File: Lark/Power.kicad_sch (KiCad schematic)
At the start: 48 parts, among them J1 54-00128, Q1 MMBT2222A-7-F, Q2 MMBT2222A-7-F, U5 SQM120P06-07L_GE3, U6 BD9E302EFJ-E2, U7 SI3474DV-T1-BE3, U8 BD9G102G-LBTR, U9 LD39200PU33R

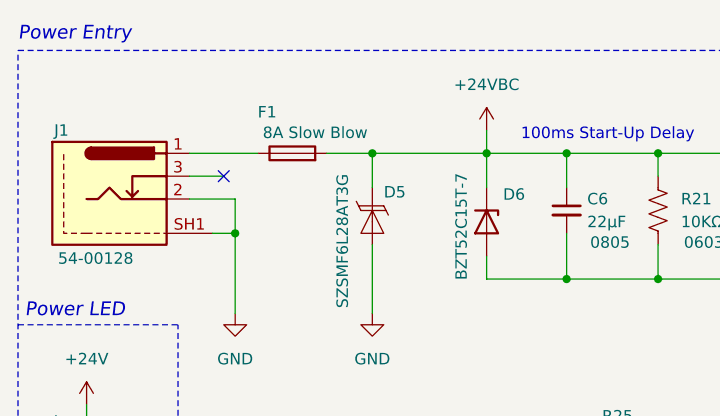
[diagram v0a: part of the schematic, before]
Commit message: Finishing up the layout, WIP
- Changed USBC footprint silkscreen.
- Routed Power Section.
- Switched from 7A to 10A Fuse.
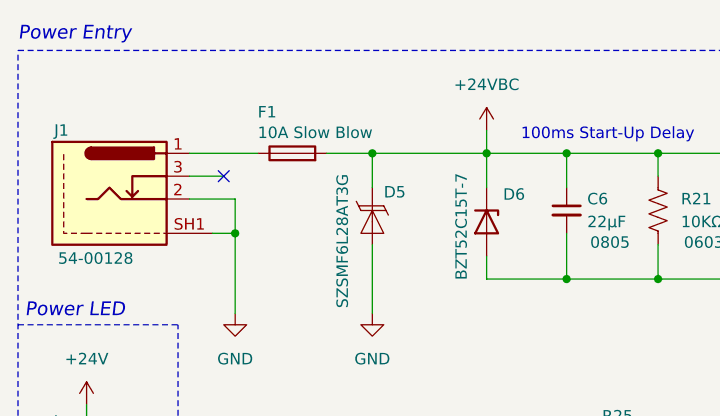
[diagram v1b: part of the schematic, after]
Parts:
- F1: value 8A Slow Blow -> 10A Slow Blow; MPN 3413.0326.22 -> 3413.0328.22
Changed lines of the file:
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@@
 			)
 		)
-		(property "Value" "8A Slow Blow"
+		(property "Value" "10A Slow Blow"
 			(at 48.26 33.274 90)
 			(effects
@@
 			)
 		)
-		(property "MPN" "3413.0326.22"
+		(property "MPN" "3413.0328.22"
 			(at 60.96 35.56 0)
 			(effects

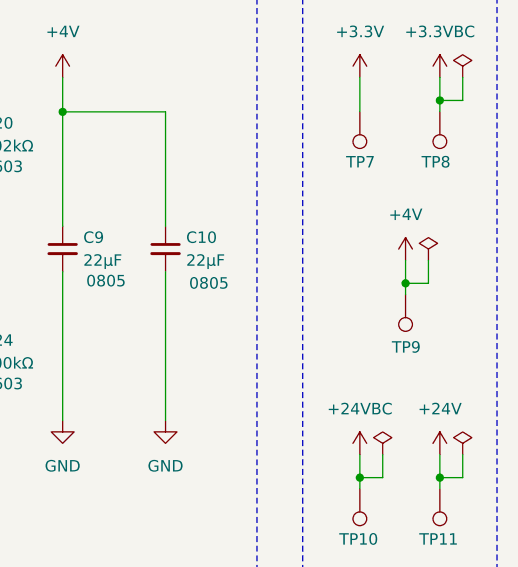
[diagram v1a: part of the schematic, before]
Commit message: minor updates
- changed npn pins to passive.
- changed rev to match working revision.
- minor PCB changes.
- moved TVS diode next to connector.
- changed barrel jack silkscreen.
- changed usbc silkscreen.
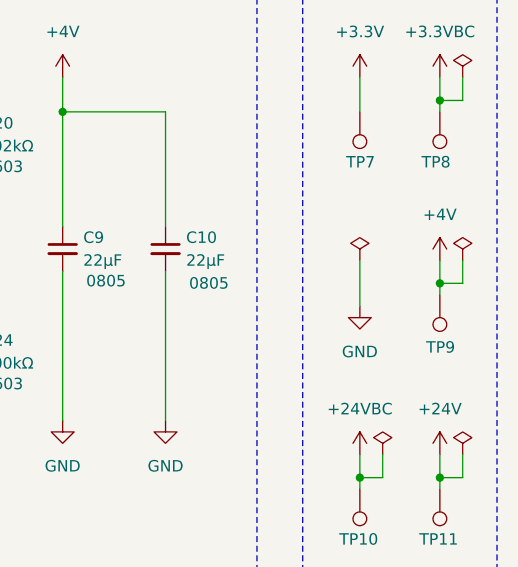
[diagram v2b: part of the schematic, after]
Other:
- moved on the sheet: TP9
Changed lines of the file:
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@@
 		(title "Lark Print Engine")
 		(date "2025-10-08")
-		(rev "01.00.01")
+		(rev "01.00.00")
 		(comment 1 "Thermal Print Engine")
 		(comment 2 "Designer: HamSlices")
@@
 	)
 	(junction
-		(at 270.51 55.88)
+		(at 274.32 55.88)
 		(diameter 0)
 		(color 0 0 0 0)
@@
 	(wire
 		(pts
-			(xy 273.05 53.34) (xy 273.05 55.88)
+			(xy 276.86 53.34) (xy 276.86 55.88)
 		)
 		(stroke
@@
 	(wire
 		(pts
-			(xy 273.05 55.88) (xy 270.51 55.88)
+			(xy 276.86 55.88) (xy 274.32 55.88)
 		)
 		(stroke
@@
 	(wire
 		(pts
-			(xy 270.51 53.34) (xy 270.51 55.88)
+			(xy 274.32 53.34) (xy 274.32 55.88)
 		)
 		(stroke
@@
 	(wire
 		(pts
-			(xy 270.51 55.88) (xy 270.51 57.15)
+			(xy 274.32 55.88) (xy 274.32 57.15)
 		)
 		(stroke
@@
 	(wire
 		(pts
+			(xy 265.43 53.34) (xy 265.43 58.42)
+		)
+		(stroke
+			(width 0)
+			(type default)
+		)
+	)
+	(wire
+		(pts
 			(xy 100.33 148.59) (xy 100.33 152.4)
 		)
@@
 	)
 	(symbol
+		(lib_id "power:PWR_FLAG")
+		(at 265.43 53.34 0)
+		(unit 1)
+		(exclude_from_sim no)
+		(in_bom yes)
+		(on_board yes)
+		(dnp no)
+		(fields_autoplaced yes)
+		(property "Reference" "#FLG07"
+			(at 265.43 51.435 0)
+			(effects
+				(font
+					(size 1.27 1.27)
+				)
+				(hide yes)
+			)
+		)
+		(property "Value" "PWR_FLAG"
+			(at 265.43 48.26 0)
+			(effects
+				(font
+					(size 1.27 1.27)
+				)
+				(hide yes)
+			)
+		)
+		(property "Footprint" ""
+			(at 265.43 53.34 0)
+			(effects
+				(font
+					(size 1.27 1.27)
+				)
+				(hide yes)
+			)
+		)
+		(property "Datasheet" "~"
+			(at 265.43 53.34 0)
+			(effects
+				(font
+					(size 1.27 1.27)
+				)
+				(hide yes)
+			)
+		)
+		(property "Description" "Special symbol for telling ERC where power comes from"
+			(at 265.43 53.34 0)
+			(effects
+				(font
+					(size 1.27 1.27)
+				)
+				(hide yes)
+			)
+		)
+		(pin "1"
+		)
+		(instances
+			(project "Lark"
+				(path "/a351af57-4353-47da-9f45-7393de572768/e2a48b8e-2a6a-42c1-ac2d-aa8bef5f3773"
+					(reference "#FLG07")
+					(unit 1)
+				)
+			)
+		)
+	)
+	(symbol
 		(lib_id "power:GND")
 		(at 218.44 152.4 0)
@@
 	)
 	(symbol
+		(lib_name "MMBT2222A-7-F_1")
 		(lib_id "Diodes Incorporated:MMBT2222A-7-F")
 		(at 215.9 144.78 0)
@@
 	(symbol
 		(lib_id "power:+3.3V")
-		(at 270.51 53.34 0)
+		(at 274.32 53.34 0)
 		(unit 1)
 		(exclude_from_sim no)
@@
 		(fields_autoplaced yes)
 		(property "Reference" "#PWR047"
-			(at 270.51 57.15 0)
+			(at 274.32 57.15 0)
 			(effects
 				(font
@@
 		)
 		(property "Value" "+4V"
-			(at 270.51 48.26 0)
+			(at 274.32 48.26 0)
 			(effects
 				(font
@@
 		)
 		(property "Footprint" ""
-			(at 270.51 53.34 0)
+			(at 274.32 53.34 0)
 			(effects
 				(font
@@
 		)
 		(property "Datasheet" ""
-			(at 270.51 53.34 0)
+			(at 274.32 53.34 0)
 			(effects
 				(font
@@
 		)
 		(property "Description" "Power symbol creates a global label with name \"+3.3V\""
-			(at 270.51 53.34 0)
+			(at 274.32 53.34 0)
 			(effects
 				(font
@@
 	)
 	(symbol
+		(lib_id "power:GND")
+		(at 265.43 58.42 0)
+		(unit 1)
+		(exclude_from_sim no)
+		(in_bom yes)
+		(on_board yes)
+		(dnp no)
+		(fields_autoplaced yes)
+		(property "Reference" "#PWR0186"
+			(at 265.43 64.77 0)
+			(effects
+				(font
+					(size 1.27 1.27)
+				)
+				(hide yes)
+			)
+		)
+		(property "Value" "GND"
+			(at 265.43 63.5 0)
+			(effects
+				(font
+					(size 1.27 1.27)
+				)
+			)
+		)
+		(property "Footprint" ""
+			(at 265.43 58.42 0)
+			(effects
+				(font
+					(size 1.27 1.27)
+				)
+				(hide yes)
+			)
+		)
+		(property "Datasheet" ""
+			(at 265.43 58.42 0)
+			(effects
+				(font
+					(size 1.27 1.27)
+				)
+				(hide yes)
+			)
+		)
+		(property "Description" "Power symbol creates a global label with name \"GND\" , ground"
+			(at 265.43 58.42 0)
+			(effects
+				(font
+					(size 1.27 1.27)
+				)
+				(hide yes)
+			)
+		)
+		(pin "1"
+		)
+		(instances
+			(project "Lark"
+				(path "/a351af57-4353-47da-9f45-7393de572768/e2a48b8e-2a6a-42c1-ac2d-aa8bef5f3773"
+					(reference "#PWR0186")
+					(unit 1)
+				)
+			)
+		)
+	)
+	(symbol
 		(lib_id "Stackpole:Resistor")
 		(at 100.33 156.21 0)
@@
 	(symbol
 		(lib_id "power:PWR_FLAG")
-		(at 273.05 53.34 0)
+		(at 276.86 53.34 0)
 		(unit 1)
 		(exclude_from_sim no)
@@
 		(fields_autoplaced yes)
 		(property "Reference" "#FLG02"
-			(at 273.05 51.435 0)
+			(at 276.86 51.435 0)
 			(effects
 				(font
@@
 		)
 		(property "Value" "PWR_FLAG"
-			(at 273.05 48.26 0)
+			(at 276.86 48.26 0)
 			(effects
 				(font
@@
 		)
 		(property "Footprint" ""
-			(at 273.05 53.34 0)
+			(at 276.86 53.34 0)
 			(effects
 				(font
@@
 		)
 		(property "Datasheet" "~"
-			(at 273.05 53.34 0)
+			(at 276.86 53.34 0)
 			(effects
 				(font
@@
 		)
 		(property "Description" "Special symbol for telling ERC where power comes from"
-			(at 273.05 53.34 0)
+			(at 276.86 53.34 0)
 			(effects
 				(font
@@
 	(symbol
 		(lib_id "Connector:TestPoint")
-		(at 270.51 57.15 180)
+		(at 274.32 57.15 180)
 		(unit 1)
 		(exclude_from_sim no)
@@
 		(dnp no)
 		(property "Reference" "TP9"
-			(at 268.986 62.992 0)
+			(at 272.796 62.992 0)
 			(effects
 				(font
@@
 		)
 		(property "Value" "TestPoint"
-			(at 268.986 65.532 0)
+			(at 272.796 65.532 0)
 			(effects
 				(font
@@
 		)
 		(property "Footprint" "TestPoint:TestPoint_Pad_D1.0mm"
-			(at 265.43 57.15 0)
+			(at 269.24 57.15 0)
 			(effects
 				(font
@@
 		)
 		(property "Datasheet" "~"
-			(at 265.43 57.15 0)
+			(at 269.24 57.15 0)
 			(effects
 				(font
@@
 		)
 		(property "Description" "test point"
-			(at 270.51 57.15 0)
+			(at 274.32 57.15 0)
 			(effects
 				(font

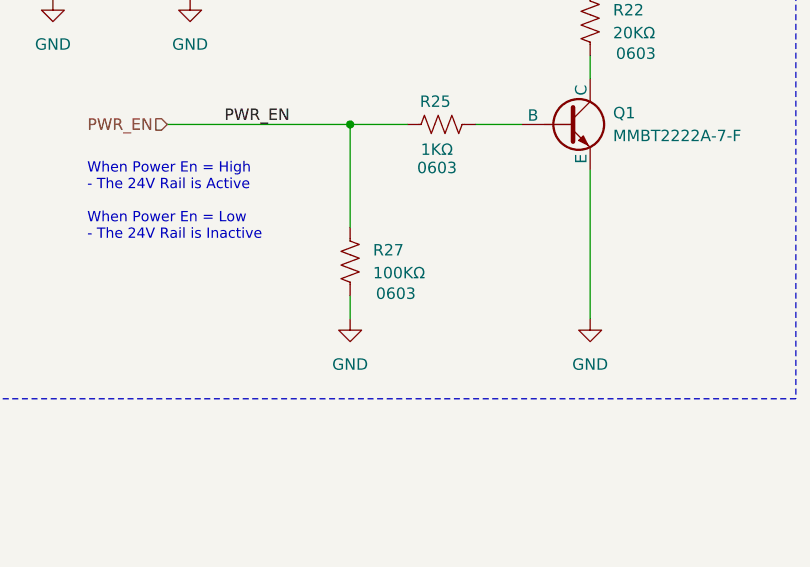
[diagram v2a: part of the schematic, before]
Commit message: Changed revision again...
- It dawned on me that this is rev 2, so the rev is now 01.00.1.
- Added thermal relief to the TH pads so I can actually solder the parts.
- Added more silkscreen to denote the rev, the github link, and ESD sensitivity of the device.
- Made minor pcb changes, I moved a test point, and cleaned up some traces.
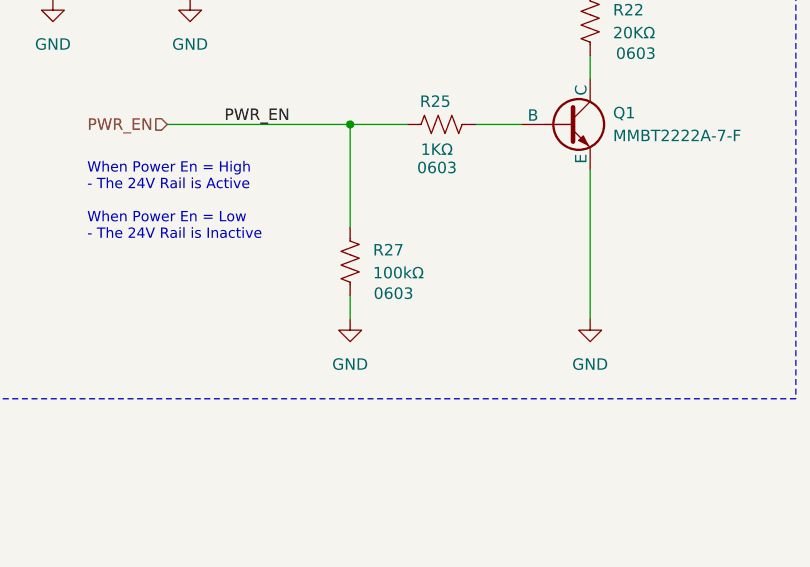
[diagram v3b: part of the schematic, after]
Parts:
- R27: value 100KΩ -> 100kΩ
- TP10, TP11, TP7, TP8, TP9: now left out of the parts list
